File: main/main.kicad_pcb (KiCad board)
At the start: 2 copper layers, 68 x 57.3 mm, 24 parts, among them IC1 MB1010-000, M1 Motor_DC, P1 Digital, P2 Analog, P3 CONN_01X01, P4 CONN_01X01, P5 CONN_01X01, P6 CONN_01X01, Q1 PN2222A, U1 SW_PWR_BTN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

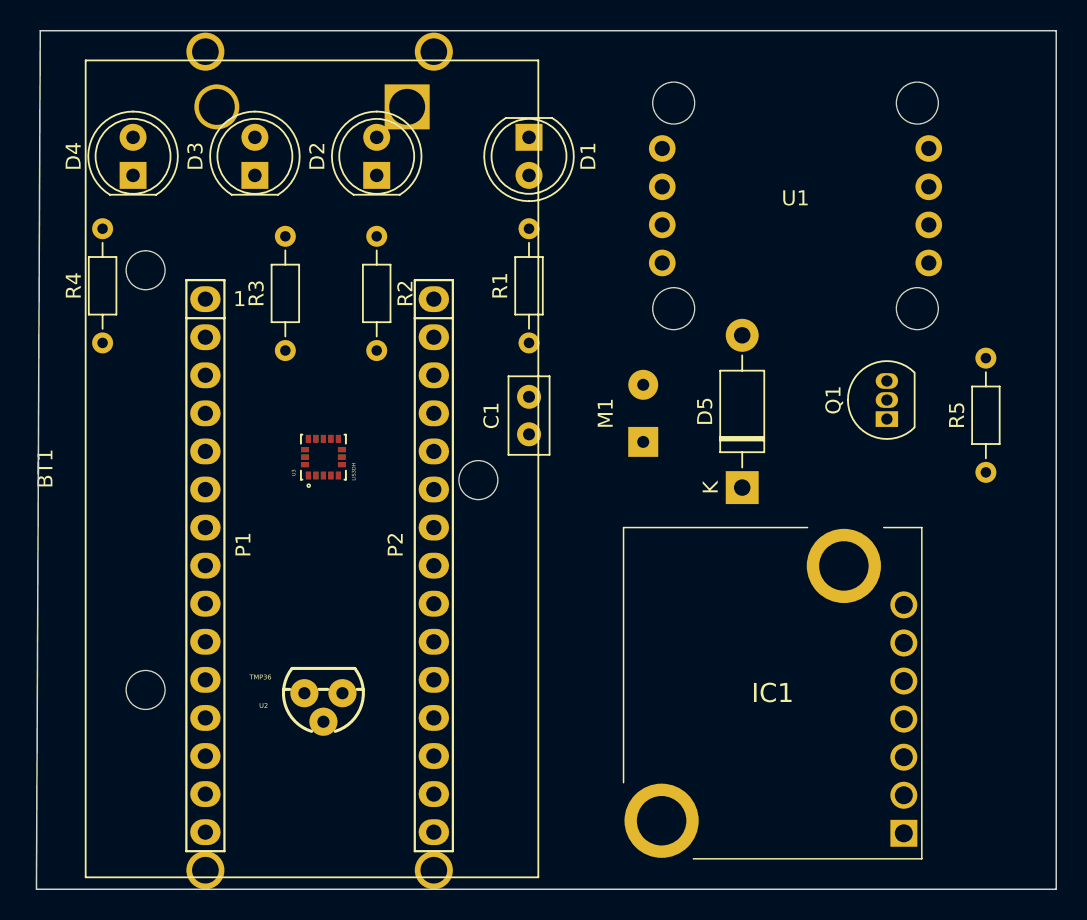
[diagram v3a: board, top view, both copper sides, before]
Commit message: pcb: Removed footprints for rangefinder sensor and push button
These were taking up a lot of room and team decided to connect
them using wires instead.
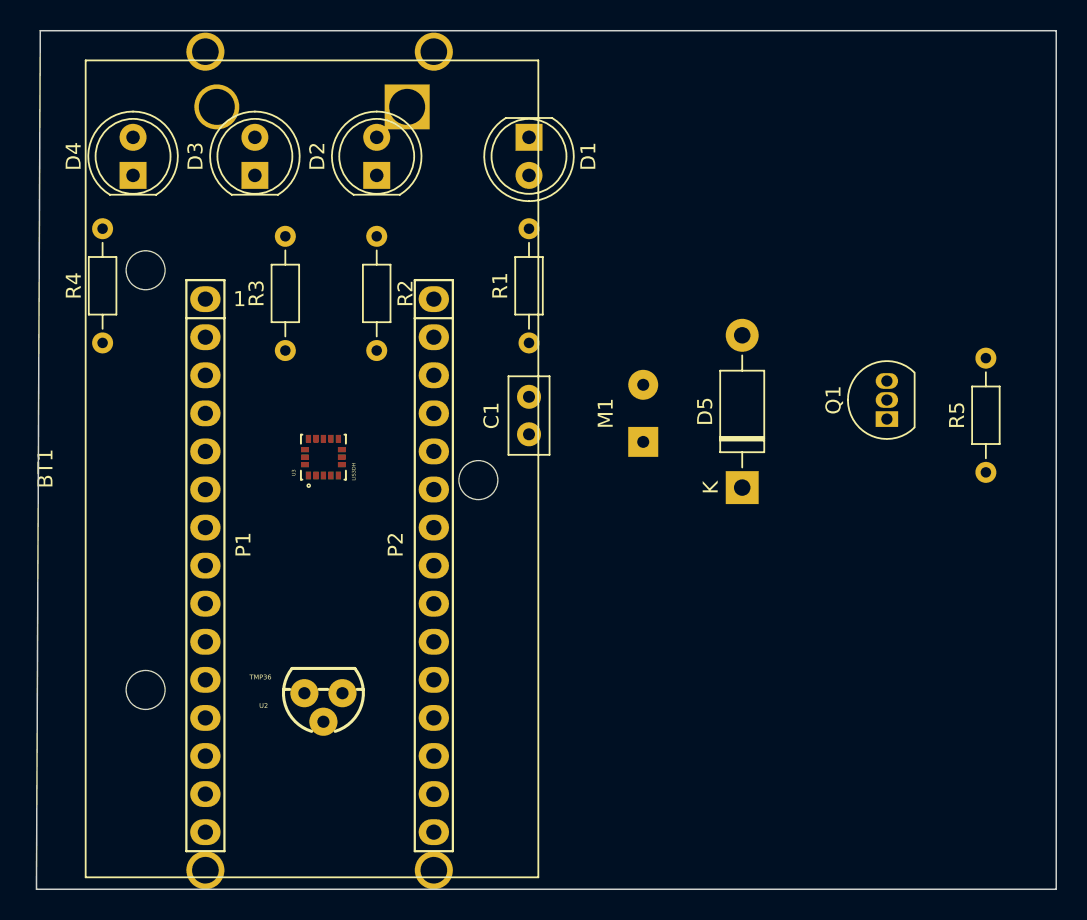
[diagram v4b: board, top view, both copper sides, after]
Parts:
- removed IC1: MB1010-000, MB1010-000:MB1010000
- removed U1: SW_PWR_BTN, 1400:1400-PWR-SW
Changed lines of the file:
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@@
     (tracks 0)
     (zones 0)
-    (modules 24)
-    (nets 59)
+    (modules 22)
+    (nets 50)
   )
   (page A4)
@@
   (net 36 "Net-(D3-Pad2)")
   (net 37 "Net-(D4-Pad2)")
-  (net 38 "Net-(IC1-Pad1)")
-  (net 39 "Net-(IC1-Pad3)")
-  (net 40 "Net-(IC1-Pad4)")
-  (net 41 "Net-(IC1-Pad5)")
-  (net 42 "Net-(IC1-Pad9)")
-  (net 43 "Net-(IC1-Pad10)")
-  (net 44 "Net-(Q1-Pad2)")
-  (net 45 "Net-(U1-Pad1)")
-  (net 46 "Net-(U1-Pad2)")
-  (net 47 "Net-(U1-Pad3)")
-  (net 48 "Net-(U3-Pad1)")
-  (net 49 "Net-(U3-Pad7)")
-  (net 50 "Net-(U3-Pad8)")
-  (net 51 "Net-(U3-Pad9)")
-  (net 52 "Net-(U3-Pad10)")
-  (net 53 "Net-(U3-Pad11)")
-  (net 54 "Net-(U3-Pad12)")
-  (net 55 "Net-(U3-Pad13)")
-  (net 56 "Net-(U3-Pad15)")
-  (net 57 "Net-(U3-Pad16)")
-  (net 58 /Battery)
+  (net 38 "Net-(Q1-Pad2)")
+  (net 39 "Net-(U3-Pad1)")
+  (net 40 "Net-(U3-Pad7)")
+  (net 41 "Net-(U3-Pad8)")
+  (net 42 "Net-(U3-Pad9)")
+  (net 43 "Net-(U3-Pad10)")
+  (net 44 "Net-(U3-Pad11)")
+  (net 45 "Net-(U3-Pad12)")
+  (net 46 "Net-(U3-Pad13)")
+  (net 47 "Net-(U3-Pad15)")
+  (net 48 "Net-(U3-Pad16)")
+  (net 49 /Battery)
   (net_class Default "This is the default net class."
     (clearance 0.2)
@@
     (add_net "Net-(D3-Pad2)")
     (add_net "Net-(D4-Pad2)")
-    (add_net "Net-(IC1-Pad1)")
-    (add_net "Net-(IC1-Pad10)")
-    (add_net "Net-(IC1-Pad3)")
-    (add_net "Net-(IC1-Pad4)")
-    (add_net "Net-(IC1-Pad5)")
-    (add_net "Net-(IC1-Pad9)")
     (add_net "Net-(P3-Pad1)")
     (add_net "Net-(P4-Pad1)")
@@
     (add_net "Net-(P6-Pad1)")
     (add_net "Net-(Q1-Pad2)")
-    (add_net "Net-(U1-Pad1)")
-    (add_net "Net-(U1-Pad2)")
-    (add_net "Net-(U1-Pad3)")
     (add_net "Net-(U3-Pad1)")
     (add_net "Net-(U3-Pad10)")
@@
     (add_net "Net-(U3-Pad8)")
     (add_net "Net-(U3-Pad9)")
-  )
-  (module 1400:1400-PWR-SW (layer F.Cu)
-    (at 178.816 65.024 180)
-    (fp_text reference U1 (at 0 0.5 180) (layer F.SilkS)
-      (effects (font (size 1 1) (thickness 0.15)))
-    )
-    (fp_text value SW_PWR_BTN (at 0 -0.5 180) (layer F.Fab)
-      (effects (font (size 1 1) (thickness 0.15)))
-    )
-    (pad 1 thru_hole circle (at 8.89005 3.828 270) (size 1.778 1.778) (drill 1.016) (layers *.Cu *.Mask)
-      (net 45 "Net-(U1-Pad1)") (solder_mask_margin 0.1016))
-    (pad 2 thru_hole circle (at 8.89005 1.27 270) (size 1.778 1.778) (drill 1.016) (layers *.Cu *.Mask)
-      (net 46 "Net-(U1-Pad2)") (solder_mask_margin 0.1016))
-    (pad 3 thru_hole circle (at 8.89005 -1.27 270) (size 1.778 1.778) (drill 1.016) (layers *.Cu *.Mask)
-      (net 47 "Net-(U1-Pad3)") (solder_mask_margin 0.1016))
-    (pad 4 thru_hole circle (at 8.89005 -3.81 270) (size 1.778 1.778) (drill 1.016) (layers *.Cu *.Mask)
-      (net 17 /A6) (solder_mask_margin 0.1016))
-    (pad "" np_thru_hole circle (at 8.12805 -6.858 180) (size 2.8 2.8) (drill 2.8) (layers *.Cu *.Mask))
-    (pad "" np_thru_hole circle (at 8.12805 6.858 180) (size 2.8 2.8) (drill 2.8) (layers *.Cu *.Mask))
-    (pad "" np_thru_hole circle (at -8.12795 6.858 180) (size 2.8 2.8) (drill 2.8) (layers *.Cu *.Mask))
-    (pad "" np_thru_hole circle (at -8.12795 -6.858 180) (size 2.8 2.8) (drill 2.8) (layers *.Cu *.Mask))
-    (pad 1 thru_hole circle (at -8.89005 3.828 270) (size 1.778 1.778) (drill 1.016) (layers *.Cu *.Mask)
-      (net 45 "Net-(U1-Pad1)") (solder_mask_margin 0.1016))
-    (pad 2 thru_hole circle (at -8.89005 1.27 270) (size 1.778 1.778) (drill 1.016) (layers *.Cu *.Mask)
-      (net 46 "Net-(U1-Pad2)") (solder_mask_margin 0.1016))
-    (pad 3 thru_hole circle (at -8.89005 -1.27 270) (size 1.778 1.778) (drill 1.016) (layers *.Cu *.Mask)
-      (net 47 "Net-(U1-Pad3)") (solder_mask_margin 0.1016))
-    (pad 4 thru_hole circle (at -8.89005 -3.81 270) (size 1.778 1.778) (drill 1.016) (layers *.Cu *.Mask)
-      (net 17 /A6) (solder_mask_margin 0.1016))
   )
   (module TMP36:TO-92 (layer F.Cu)
@@
     (pad "" np_thru_hole circle (at -10.9 -17.45 90) (size 2.6 2.6) (drill 2.6) (layers *.Cu *.Mask))
     (pad 1 thru_hole rect (at 0 0 90) (size 3 3) (drill 2.4) (layers *.Cu *.Mask)
-      (net 58 /Battery))
+      (net 49 /Battery))
     (pad 2 thru_hole circle (at 0 -12.7 90) (size 3 3) (drill 2.4) (layers *.Cu *.Mask)
       (net 4 GND))
@@
     )
   )
-  (module MB1010-000:MB1010000 (layer F.Cu)
-    (at 177.292 97.536 180)
-    (descr MB1010-000)
-    (tags "Integrated Circuit")
-    (fp_text reference IC1 (at 0 0 180) (layer F.SilkS)
-      (effects (font (size 1.27 1.27) (thickness 0.254)))
-    )
-    (fp_text value MB1010-000 (at 0 0 180) (layer F.SilkS) hide
-      (effects (font (size 1.27 1.27) (thickness 0.254)))
-    )
-    (fp_line (start 9.95 11.05) (end 9.95 -5.97) (layer F.SilkS) (width 0.1))
-    (fp_line (start -2.33 11.05) (end 9.95 11.05) (layer F.SilkS) (width 0.1))
-    (fp_line (start -9.95 11.05) (end -7.41 11.05) (layer F.SilkS) (width 0.1))
-    (fp_line (start -9.95 -11.05) (end -9.95 11.05) (layer F.SilkS) (width 0.1))
-    (fp_line (start 5.29 -11.05) (end -9.95 -11.05) (layer F.SilkS) (width 0.1))
-    (fp_line (start -10.95 -12.05) (end -10.95 12.05) (layer Dwgs.User) (width 0.1))
-    (fp_line (start 10.95 -12.05) (end -10.95 -12.05) (layer Dwgs.User) (width 0.1))
-    (fp_line (start 10.95 12.05) (end 10.95 -12.05) (layer Dwgs.User) (width 0.1))
-    (fp_line (start -10.95 12.05) (end 10.95 12.05) (layer Dwgs.User) (width 0.1))
-    (fp_line (start -9.95 -11.05) (end -9.95 11.05) (layer Dwgs.User) (width 0.2))
-    (fp_line (start 9.95 -11.05) (end -9.95 -11.05) (layer Dwgs.User) (width 0.2))
-    (fp_line (start 9.95 11.05) (end 9.95 -11.05) (layer Dwgs.User) (width 0.2))
-    (fp_line (start -9.95 11.05) (end 9.95 11.05) (layer Dwgs.User) (width 0.2))
-    (pad 10 thru_hole circle (at 7.41 -8.51 270) (size 4.95 4.95) (drill 3.3) (layers *.Cu *.Mask F.SilkS)
-      (net 43 "Net-(IC1-Pad10)"))
-    (pad 9 thru_hole circle (at -4.75 8.49 270) (size 4.95 4.95) (drill 3.3) (layers *.Cu *.Mask F.SilkS)
-      (net 42 "Net-(IC1-Pad9)"))
-    (pad 7 thru_hole circle (at -8.75 5.89 270) (size 1.8 1.8) (drill 1.2) (layers *.Cu *.Mask F.SilkS)
-      (net 4 GND))
-    (pad 6 thru_hole circle (at -8.75 3.35 270) (size 1.8 1.8) (drill 1.2) (layers *.Cu *.Mask F.SilkS)
-      (net 15 +5V))
-    (pad 5 thru_hole circle (at -8.75 0.81 270) (size 1.8 1.8) (drill 1.2) (layers *.Cu *.Mask F.SilkS)
-      (net 41 "Net-(IC1-Pad5)"))
-    (pad 4 thru_hole circle (at -8.75 -1.73 270) (size 1.8 1.8) (drill 1.2) (layers *.Cu *.Mask F.SilkS)
-      (net 40 "Net-(IC1-Pad4)"))
-    (pad 3 thru_hole circle (at -8.75 -4.27 270) (size 1.8 1.8) (drill 1.2) (layers *.Cu *.Mask F.SilkS)
-      (net 39 "Net-(IC1-Pad3)"))
-    (pad 2 thru_hole circle (at -8.75 -6.81 270) (size 1.8 1.8) (drill 1.2) (layers *.Cu *.Mask F.SilkS)
-      (net 5 /2))
-    (pad 1 thru_hole rect (at -8.75 -9.35 270) (size 1.8 1.8) (drill 1.2) (layers *.Cu *.Mask F.SilkS)
-      (net 38 "Net-(IC1-Pad1)"))
-  )
   (module Connector_Wire:SolderWirePad_1x02_P3.81mm_Drill0.8mm (layer F.Cu)
     (at 168.656 80.772 90)
@@
     (fp_arc (start 1.27 0) (end 1.27 -2.6) (angle 135) (layer F.SilkS) (width 0.12))
     (pad 2 thru_hole oval (at 1.27 0 90) (size 1.05 1.5) (drill 0.75) (layers *.Cu *.Mask)
-      (net 44 "Net-(Q1-Pad2)"))
+      (net 38 "Net-(Q1-Pad2)"))
     (pad 3 thru_hole oval (at 2.54 0 90) (size 1.05 1.5) (drill 0.75) (layers *.Cu *.Mask)
       (net 33 "Net-(C1-Pad2)"))
@@
       (net 10 /7))
     (pad 2 thru_hole oval (at 7.62 0 90) (size 1.4 1.4) (drill 0.7) (layers *.Cu *.Mask)
-      (net 44 "Net-(Q1-Pad2)"))
+      (net 38 "Net-(Q1-Pad2)"))
     (model ${KISYS3DMOD}/Resistor_THT.3dshapes/R_Axial_DIN0204_L3.6mm_D1.6mm_P7.62mm_Horizontal.wrl
       (at (xyz 0 0 0))
@@
     (fp_line (start 1.5 1.5) (end 1.5 1.4) (layer F.SilkS) (width 0.127))
     (pad 1 smd rect (at -1.225 -1 90) (size 0.52 0.35) (layers F.Cu F.Paste F.Mask)
-      (net 48 "Net-(U3-Pad1)"))
+      (net 39 "Net-(U3-Pad1)"))
     (pad 2 smd rect (at -1.225 -0.5 90) (size 0.52 0.35) (layers F.Cu F.Paste F.Mask))
     (pad 3 smd rect (at -1.225 0 90) (size 0.52 0.35) (layers F.Cu F.Paste F.Mask))
@@
       (net 19 /A4))
     (pad 7 smd rect (at 0 1.225 180) (size 0.52 0.35) (layers F.Cu F.Paste F.Mask)
-      (net 49 "Net-(U3-Pad7)"))
+      (net 40 "Net-(U3-Pad7)"))
     (pad 8 smd rect (at 0.5 1.225 180) (size 0.52 0.35) (layers F.Cu F.Paste F.Mask)
-      (net 50 "Net-(U3-Pad8)"))
+      (net 41 "Net-(U3-Pad8)"))
     (pad 9 smd rect (at 1.225 1 270) (size 0.52 0.35) (layers F.Cu F.Paste F.Mask)
-      (net 51 "Net-(U3-Pad9)"))
+      (net 42 "Net-(U3-Pad9)"))
     (pad 10 smd rect (at 1.225 0.5 270) (size 0.52 0.35) (layers F.Cu F.Paste F.Mask)
-      (net 52 "Net-(U3-Pad10)"))
+      (net 43 "Net-(U3-Pad10)"))
     (pad 11 smd rect (at 1.225 0 270) (size 0.52 0.35) (layers F.Cu F.Paste F.Mask)
-      (net 53 "Net-(U3-Pad11)"))
+      (net 44 "Net-(U3-Pad11)"))
     (pad 12 smd rect (at 1.225 -0.5 270) (size 0.52 0.35) (layers F.Cu F.Paste F.Mask)
-      (net 54 "Net-(U3-Pad12)"))
+      (net 45 "Net-(U3-Pad12)"))
     (pad 13 smd rect (at 1.225 -1 270) (size 0.52 0.35) (layers F.Cu F.Paste F.Mask)
-      (net 55 "Net-(U3-Pad13)"))
+      (net 46 "Net-(U3-Pad13)"))
     (pad 14 smd rect (at 0.5 -1.225 180) (size 0.52 0.35) (layers F.Cu F.Paste F.Mask)
       (net 15 +5V))
     (pad 15 smd rect (at 0 -1.225 180) (size 0.52 0.35) (layers F.Cu F.Paste F.Mask)
-      (net 56 "Net-(U3-Pad15)"))
+      (net 47 "Net-(U3-Pad15)"))
     (pad 16 smd rect (at -0.5 -1.225 180) (size 0.52 0.35) (layers F.Cu F.Paste F.Mask)
-      (net 57 "Net-(U3-Pad16)"))
+      (net 48 "Net-(U3-Pad16)"))
   )
   (gr_text 1 (at 141.732 71.247) (layer F.SilkS)

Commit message: pcb: Performed layout of components to minimize size
The current layout closely matches size of battery holder footprint.
This arrangement does not yet have traces added.
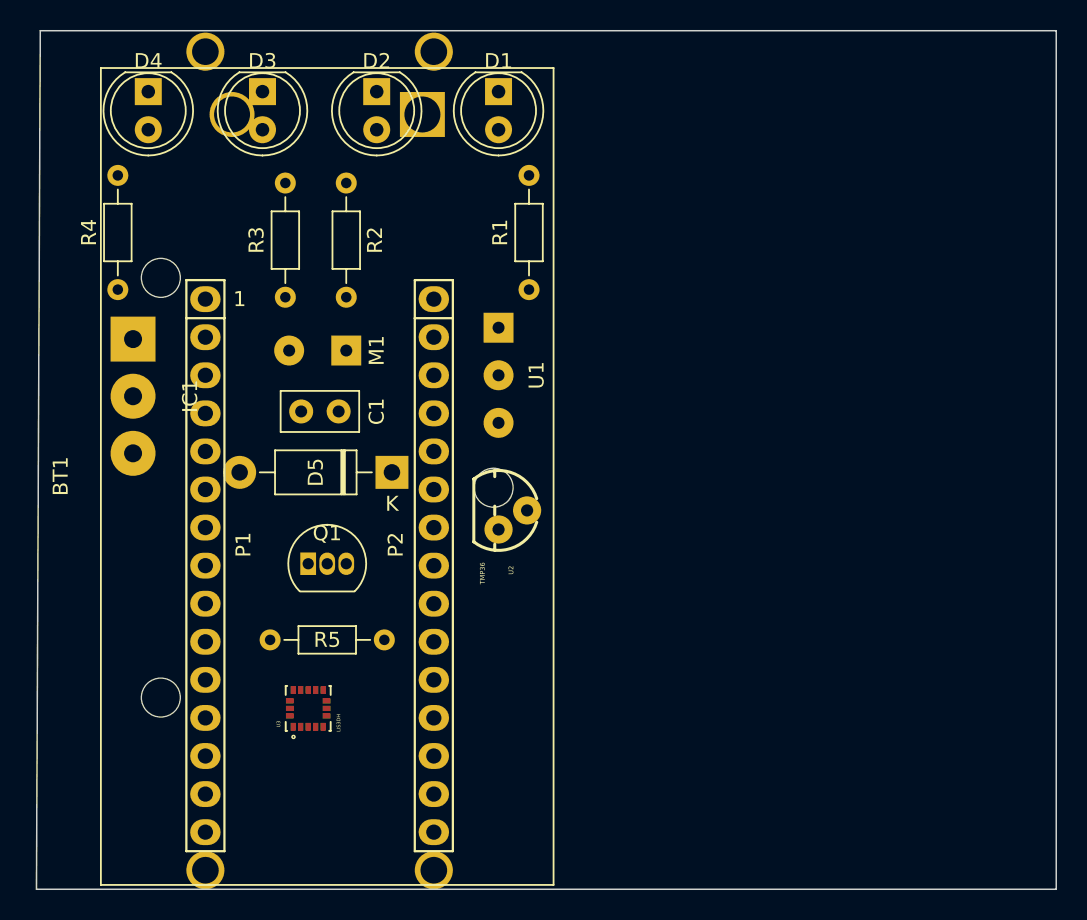
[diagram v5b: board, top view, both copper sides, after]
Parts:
- added IC1: MB1010-000, Connector_Wire:SolderWirePad_1x03_P3.81mm_Drill1.2mm, F.Cu at (134.6, 73.9)
- added U1: SW_PWR_BTN, Connector_Wire:SolderWirePad_1x03_P3.175mm_Drill0.8mm, F.Cu at (159.0, 73.2)
- moved R5 49.0 mm to (143.8, 94.0), turned to 0 degrees
- moved Q1 39.8 mm to (146.3, 88.9), turned to 0 degrees
- moved D5 23.4 mm to (151.9, 82.8), turned to 180 degrees
- moved M1 20.7 mm to (148.8, 74.7), turned to 180 degrees
- moved U2 16.9 mm to (159.0, 85.3), turned to 270 degrees
- moved U3 16.8 mm to (146.3, 98.6)
- moved C1 12.8 mm to (148.3, 78.7), turned to 180 degrees
- moved D4 5.68 mm to (135.6, 57.4), turned to 270 degrees
- moved D3 5.61 mm to (143.3, 57.4), turned to 270 degrees
- moved D2 5.59 mm to (150.9, 57.4), turned to 270 degrees
- moved R2 4.10 mm to (148.8, 63.5)
- moved R4 3.70 mm to (133.6, 70.6)
- moved D1 3.66 mm to (159.0, 57.4)
- moved R1 3.56 mm to (161.0, 70.6)
- moved R3 3.56 mm to (144.8, 71.1)
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
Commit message: pcb: Fixed mismatching endpoints of board outline
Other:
- board size 68 x 57.3 mm -> 31.2 x 57.3 mm
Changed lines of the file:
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@@
   (gr_line (start 143.256 72.517) (end 150.876 72.517) (angle 90) (layer Dwgs.User) (width 0.15))
   (gr_line (start 143.256 67.437) (end 143.256 72.517) (angle 90) (layer Dwgs.User) (width 0.15))
-  (gr_line (start 128.43 53.34) (end 128.176 110.617) (angle 90) (layer Edge.Cuts) (width 0.1))
-  (gr_line (start 196.21 53.34) (end 128.43 53.34) (angle 90) (layer Edge.Cuts) (width 0.1))
-  (gr_line (start 196.21 110.617) (end 196.21 53.34) (angle 90) (layer Edge.Cuts) (width 0.1))
-  (gr_line (start 128.176 110.617) (end 196.21 110.617) (angle 90) (layer Edge.Cuts) (width 0.1))
+  (gr_line (start 131.826 53.34) (end 131.826 110.617) (angle 90) (layer Edge.Cuts) (width 0.1))
+  (gr_line (start 163.068 53.34) (end 131.826 53.34) (angle 90) (layer Edge.Cuts) (width 0.1))
+  (gr_line (start 163.068 110.617) (end 163.068 53.34) (angle 90) (layer Edge.Cuts) (width 0.1))
+  (gr_line (start 131.826 110.617) (end 163.068 110.617) (angle 90) (layer Edge.Cuts) (width 0.1))
 )
